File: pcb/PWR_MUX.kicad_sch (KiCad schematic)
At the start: 6 parts, among them IC7 TPS2121RUXT

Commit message: power done
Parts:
- added JP3: SolderJumper_2_Bridged, Jumper:SolderJumper-2_P1.3mm_Bridged_RoundedPad1.0x1.5mm, symbol Jumper:SolderJumper_2_Bridged
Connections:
- net GND: now also JP3.2 (B); no longer IC7.3 (CP2)
- new net: IC7.3 (CP2), JP3.1 (A)
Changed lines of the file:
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@@
 	(wire
 		(pts
-			(xy 111.76 76.2) (xy 114.3 76.2)
+			(xy 111.76 76.2) (xy 115.57 76.2)
 		)
 		(stroke
@@
 		(pts
 			(xy 76.2 60.96) (xy 83.82 60.96)
+		)
+		(stroke
+			(width 0)
+			(type default)
+		)
+	)
+	(wire
+		(pts
+			(xy 123.19 76.2) (xy 127 76.2)
 		)
 		(stroke
@@
 	(symbol
 		(lib_id "power:GND")
-		(at 114.3 76.2 90)
+		(at 127 76.2 90)
 		(unit 1)
 		(exclude_from_sim no)
@@
 		(dnp no)
 		(property "Reference" "#PWR0306"
-			(at 120.65 76.2 0)
+			(at 133.35 76.2 0)
 			(effects
 				(font
@@
 		)
 		(property "Value" "GND"
-			(at 118.11 76.2 0)
+			(at 130.81 76.2 0)
 			(effects
 				(font
@@
 		)
 		(property "Footprint" ""
-			(at 114.3 76.2 0)
+			(at 127 76.2 0)
 			(effects
 				(font
@@
 		)
 		(property "Datasheet" ""
-			(at 114.3 76.2 0)
+			(at 127 76.2 0)
 			(effects
 				(font
@@
 		)
 		(property "Description" "Power symbol creates a global label with name \"GND\" , ground"
-			(at 114.3 76.2 0)
+			(at 127 76.2 0)
 			(effects
 				(font
@@
 					(unit 1)
 				)
+			)
+		)
+	)
+	(symbol
+		(lib_id "Jumper:SolderJumper_2_Bridged")
+		(at 119.38 76.2 0)
+		(unit 1)
+		(exclude_from_sim no)
+		(in_bom no)
+		(on_board yes)
+		(dnp no)
+		(property "Reference" "JP3"
+			(at 119.38 73.66 0)
+			(effects
+				(font
+					(size 1.27 1.27)
+				)
+			)
+		)
+		(property "Value" "SolderJumper_2_Bridged"
+			(at 119.38 72.39 0)
+			(effects
+				(font
+					(size 1.27 1.27)
+				)
+				(hide yes)
+			)
+		)
+		(property "Footprint" "Jumper:SolderJumper-2_P1.3mm_Bridged_RoundedPad1.0x1.5mm"
+			(at 119.38 76.2 0)
+			(effects
+				(font
+					(size 1.27 1.27)
+				)
+				(hide yes)
+			)
+		)
+		(property "Datasheet" "~"
+			(at 119.38 76.2 0)
+			(effects
+				(font
+					(size 1.27 1.27)
+				)
+				(hide yes)
+			)
+		)
+		(property "Description" "Solder Jumper, 2-pole, closed/bridged"
+			(at 119.38 76.2 0)
+			(effects
+				(font
+					(size 1.27 1.27)
+				)
+				(hide yes)
+			)
+		)
+		(pin "1"
+		)
+		(pin "2"
+		)
+		(instances
+			(project ""
+				(path "/3aee14c3-5480-4f7c-989e-3fef81779034/05e3be97-98f6-4518-a1a7-240d4da327e6/d1a8c66e-d7c5-4f43-8cdd-a3ddabbe33e6"
+					(reference "JP3")
+					(unit 1)
+				)

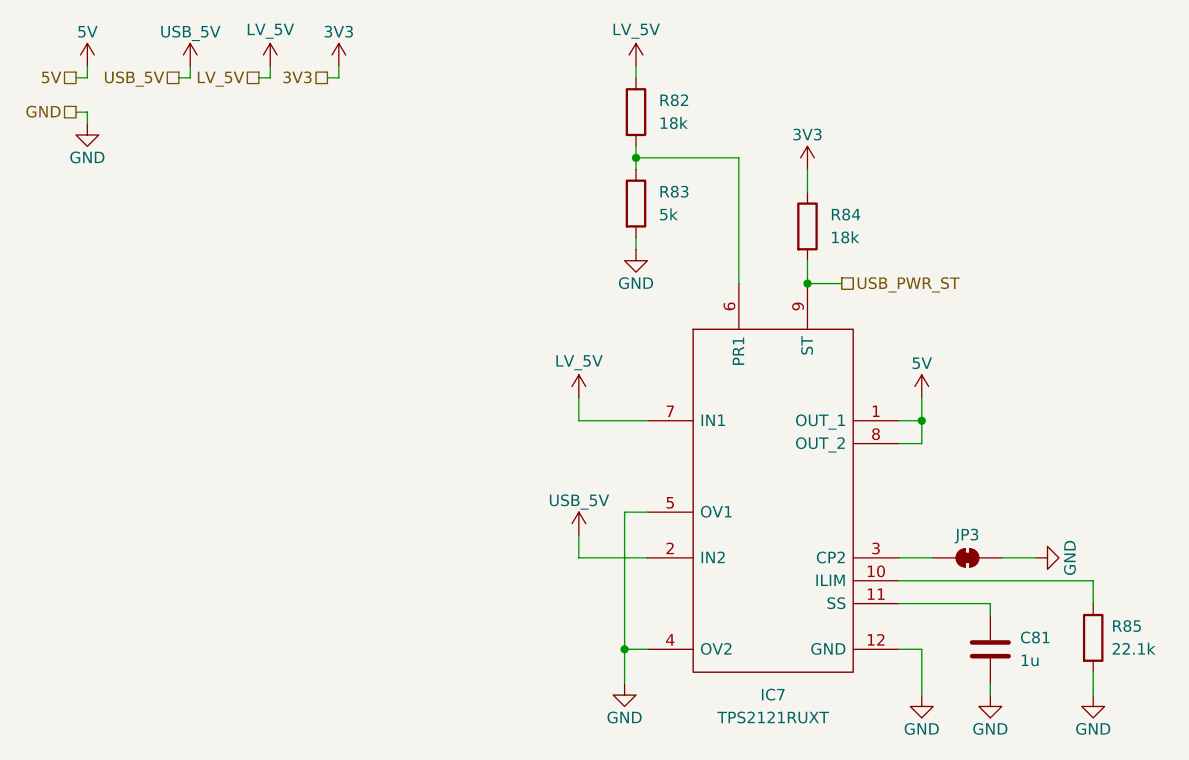
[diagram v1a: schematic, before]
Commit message: reannotated, updated some symbols
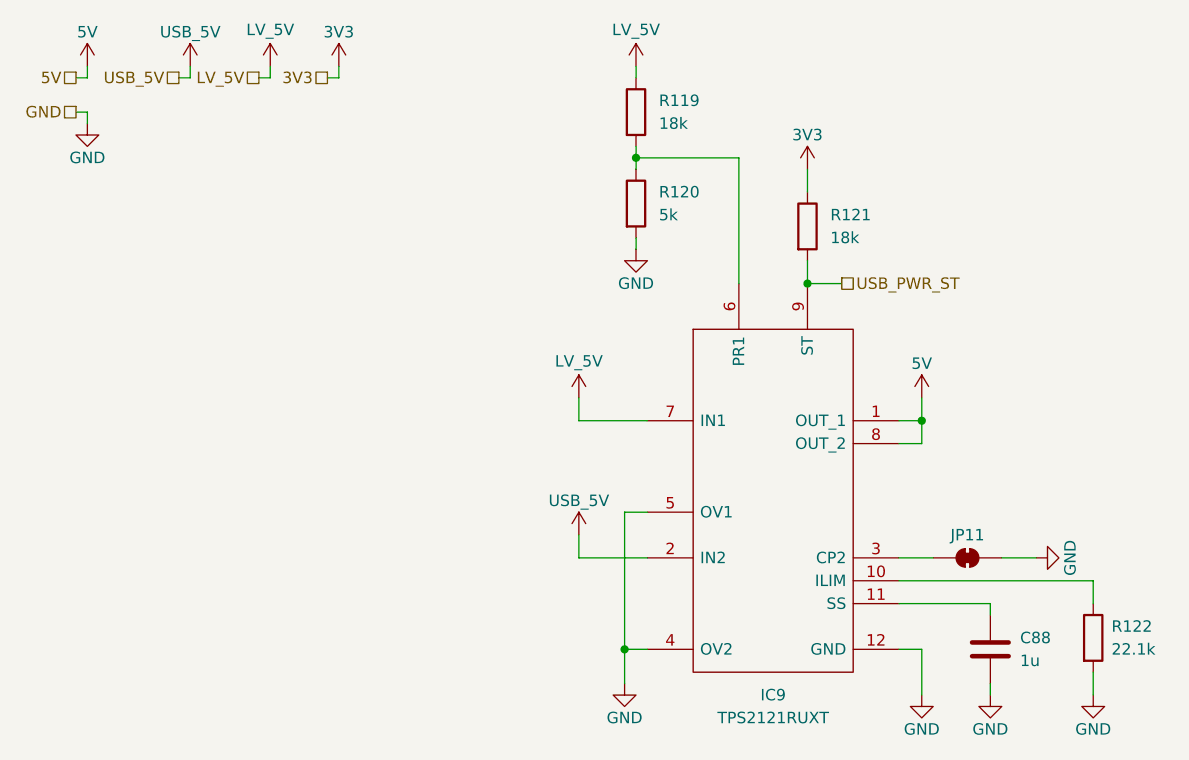
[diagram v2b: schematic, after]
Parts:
- renumbered C81 to C88, IC7 to IC9, JP3 to JP11, R82 to R119, R83 to R120, R84 to R121, R85 to R122
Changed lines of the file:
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@@
 		(on_board yes)
 		(dnp no)
-		(property "Reference" "C81"
+		(property "Reference" "C88"
 			(at 125.222 85.09 0)
 			(effects
@@
 			(project ""
 				(path "/3aee14c3-5480-4f7c-989e-3fef81779034/05e3be97-98f6-4518-a1a7-240d4da327e6/d1a8c66e-d7c5-4f43-8cdd-a3ddabbe33e6"
-					(reference "C81")
+					(reference "C88")
 					(unit 1)
 				)
@@
 		(dnp no)
 		(fields_autoplaced yes)
-		(property "Reference" "R84"
+		(property "Reference" "R121"
 			(at 104.14 38.0999 0)
 			(effects
@@
 			(project "NCU"
 				(path "/3aee14c3-5480-4f7c-989e-3fef81779034/05e3be97-98f6-4518-a1a7-240d4da327e6/d1a8c66e-d7c5-4f43-8cdd-a3ddabbe33e6"
-					(reference "R84")
+					(reference "R121")
 					(unit 1)
 				)
@@
 		(on_board yes)
 		(dnp no)
-		(property "Reference" "#PWR0303"
+		(property "Reference" "#PWR0399"
 			(at 82.55 48.26 0)
 			(effects
@@
 			(project "NCU"
 				(path "/3aee14c3-5480-4f7c-989e-3fef81779034/05e3be97-98f6-4518-a1a7-240d4da327e6/d1a8c66e-d7c5-4f43-8cdd-a3ddabbe33e6"
-					(reference "#PWR0303")
+					(reference "#PWR0399")
 					(unit 1)
 				)
@@
 		(on_board yes)
 		(dnp no)
-		(property "Reference" "#PWR0306"
+		(property "Reference" "#PWR0404"
 			(at 133.35 76.2 0)
 			(effects
@@
 			(project "NCU"
 				(path "/3aee14c3-5480-4f7c-989e-3fef81779034/05e3be97-98f6-4518-a1a7-240d4da327e6/d1a8c66e-d7c5-4f43-8cdd-a3ddabbe33e6"
-					(reference "#PWR0306")
+					(reference "#PWR0404")
 					(unit 1)
 				)
@@
 		(on_board yes)
 		(dnp no)
-		(property "Reference" "#PWR0294"
+		(property "Reference" "#PWR0390"
 			(at 21.59 25.4 0)
 			(effects
@@
 			(project "NCU"
 				(path "/3aee14c3-5480-4f7c-989e-3fef81779034/05e3be97-98f6-4518-a1a7-240d4da327e6/d1a8c66e-d7c5-4f43-8cdd-a3ddabbe33e6"
-					(reference "#PWR0294")
+					(reference "#PWR0390")
 					(unit 1)
 				)
@@
 		(on_board yes)
 		(dnp no)
-		(property "Reference" "#PWR0308"
+		(property "Reference" "#PWR0403"
 			(at 121.92 97.79 0)
 			(effects
@@
 			(project "NCU"
 				(path "/3aee14c3-5480-4f7c-989e-3fef81779034/05e3be97-98f6-4518-a1a7-240d4da327e6/d1a8c66e-d7c5-4f43-8cdd-a3ddabbe33e6"
-					(reference "#PWR0308")
+					(reference "#PWR0403")
 					(unit 1)
 				)
@@
 		(on_board yes)
 		(dnp no)
-		(property "Reference" "#PWR0304"
+		(property "Reference" "#PWR0400"
 			(at 101.6 36.83 0)
 			(effects
@@
 			(project "NCU"
 				(path "/3aee14c3-5480-4f7c-989e-3fef81779034/05e3be97-98f6-4518-a1a7-240d4da327e6/d1a8c66e-d7c5-4f43-8cdd-a3ddabbe33e6"
-					(reference "#PWR0304")
+					(reference "#PWR0400")
 					(unit 1)
 				)
@@
 		(on_board yes)
 		(dnp no)
-		(property "Reference" "#PWR0307"
+		(property "Reference" "#PWR0402"
 			(at 114.3 97.79 0)
 			(effects
@@
 			(project "NCU"
 				(path "/3aee14c3-5480-4f7c-989e-3fef81779034/05e3be97-98f6-4518-a1a7-240d4da327e6/d1a8c66e-d7c5-4f43-8cdd-a3ddabbe33e6"
-					(reference "#PWR0307")
+					(reference "#PWR0402")
 					(unit 1)
 				)
@@
 		(on_board yes)
 		(dnp no)
-		(property "Reference" "R85"
+		(property "Reference" "R122"
 			(at 135.382 83.82 0)
 			(effects
@@
 			(project "NCU"
 				(path "/3aee14c3-5480-4f7c-989e-3fef81779034/05e3be97-98f6-4518-a1a7-240d4da327e6/d1a8c66e-d7c5-4f43-8cdd-a3ddabbe33e6"
-					(reference "R85")
+					(reference "R122")
 					(unit 1)
 				)
@@
 		(on_board yes)
 		(dnp no)
-		(property "Reference" "JP3"
+		(property "Reference" "JP11"
 			(at 119.38 73.66 0)
 			(effects
@@
 			(project ""
 				(path "/3aee14c3-5480-4f7c-989e-3fef81779034/05e3be97-98f6-4518-a1a7-240d4da327e6/d1a8c66e-d7c5-4f43-8cdd-a3ddabbe33e6"
-					(reference "JP3")
+					(reference "JP11")
 					(unit 1)
 				)
@@
 		(on_board yes)
 		(dnp no)
-		(property "Reference" "#PWR0302"
+		(property "Reference" "#PWR0398"
 			(at 82.55 25.4 0)
 			(effects
@@
 			(project "NCU"
 				(path "/3aee14c3-5480-4f7c-989e-3fef81779034/05e3be97-98f6-4518-a1a7-240d4da327e6/d1a8c66e-d7c5-4f43-8cdd-a3ddabbe33e6"
-					(reference "#PWR0302")
+					(reference "#PWR0398")
 					(unit 1)
 				)
@@
 		(on_board yes)
 		(dnp no)
-		(property "Reference" "#PWR0309"
+		(property "Reference" "#PWR0405"
 			(at 133.35 97.79 0)
 			(effects
@@
 			(project "NCU"
 				(path "/3aee14c3-5480-4f7c-989e-3fef81779034/05e3be97-98f6-4518-a1a7-240d4da327e6/d1a8c66e-d7c5-4f43-8cdd-a3ddabbe33e6"
-					(reference "#PWR0309")
+					(reference "#PWR0405")
 					(unit 1)
 				)
@@
 		(dnp no)
 		(fields_autoplaced yes)
-		(property "Reference" "R83"
+		(property "Reference" "R120"
 			(at 85.09 35.5599 0)
 			(effects
@@
 			(project "NCU"
 				(path "/3aee14c3-5480-4f7c-989e-3fef81779034/05e3be97-98f6-4518-a1a7-240d4da327e6/d1a8c66e-d7c5-4f43-8cdd-a3ddabbe33e6"
-					(reference "R83")
+					(reference "R120")
 					(unit 1)
 				)
@@
 		(on_board yes)
 		(dnp no)
-		(property "Reference" "#PWR0298"
+		(property "Reference" "#PWR0394"
 			(at 49.53 25.4 0)
 			(effects
@@
 			(project "NCU"
 				(path "/3aee14c3-5480-4f7c-989e-3fef81779034/05e3be97-98f6-4518-a1a7-240d4da327e6/d1a8c66e-d7c5-4f43-8cdd-a3ddabbe33e6"
-					(reference "#PWR0298")
+					(reference "#PWR0394")
 					(unit 1)
 				)
@@
 		(on_board yes)
 		(dnp no)
-		(property "Reference" "#PWR0297"
+		(property "Reference" "#PWR0393"
 			(at 41.91 25.4 0)
 			(effects
@@
 			(project "NCU"
 				(path "/3aee14c3-5480-4f7c-989e-3fef81779034/05e3be97-98f6-4518-a1a7-240d4da327e6/d1a8c66e-d7c5-4f43-8cdd-a3ddabbe33e6"
-					(reference "#PWR0297")
+					(reference "#PWR0393")
 					(unit 1)
 				)
@@
 		(dnp no)
 		(fields_autoplaced yes)
-		(property "Reference" "R82"
+		(property "Reference" "R119"
 			(at 85.09 25.3999 0)
 			(effects
@@
 			(project ""
 				(path "/3aee14c3-5480-4f7c-989e-3fef81779034/05e3be97-98f6-4518-a1a7-240d4da327e6/d1a8c66e-d7c5-4f43-8cdd-a3ddabbe33e6"
-					(reference "R82")
+					(reference "R119")
 					(unit 1)
 				)
@@
 		(dnp no)
 		(fields_autoplaced yes)
-		(property "Reference" "IC7"
+		(property "Reference" "IC9"
 			(at 97.79 91.44 0)
 			(effects
@@
 			(project ""
 				(path "/3aee14c3-5480-4f7c-989e-3fef81779034/05e3be97-98f6-4518-a1a7-240d4da327e6/d1a8c66e-d7c5-4f43-8cdd-a3ddabbe33e6"
-					(reference "IC7")
+					(reference "IC9")
 					(unit 1)
 				)
@@
 		(on_board yes)
 		(dnp no)
-		(property "Reference" "#PWR0299"
+		(property "Reference" "#PWR0395"
 			(at 76.2 62.23 0)
 			(effects
@@
 			(project "NCU"
 				(path "/3aee14c3-5480-4f7c-989e-3fef81779034/05e3be97-98f6-4518-a1a7-240d4da327e6/d1a8c66e-d7c5-4f43-8cdd-a3ddabbe33e6"
-					(reference "#PWR0299")
+					(reference "#PWR0395")
 					(unit 1)
 				)
@@
 		(on_board yes)
 		(dnp no)
-		(property "Reference" "#PWR0296"
+		(property "Reference" "#PWR0392"
 			(at 33.02 25.4 0)
 			(effects
@@
 			(project "NCU"
 				(path "/3aee14c3-5480-4f7c-989e-3fef81779034/05e3be97-98f6-4518-a1a7-240d4da327e6/d1a8c66e-d7c5-4f43-8cdd-a3ddabbe33e6"
-					(reference "#PWR0296")
+					(reference "#PWR0392")
 					(unit 1)
 				)
@@
 		(on_board yes)
 		(dnp no)
-		(property "Reference" "#PWR0301"
+		(property "Reference" "#PWR0397"
 			(at 81.28 96.52 0)
 			(effects
@@
 			(project "NCU"
 				(path "/3aee14c3-5480-4f7c-989e-3fef81779034/05e3be97-98f6-4518-a1a7-240d4da327e6/d1a8c66e-d7c5-4f43-8cdd-a3ddabbe33e6"
-					(reference "#PWR0301")
+					(reference "#PWR0397")
 					(unit 1)
 				)
@@
 		(on_board yes)
 		(dnp no)
-		(property "Reference" "#PWR0295"
+		(property "Reference" "#PWR0391"
 			(at 21.59 34.29 0)
 			(effects
@@
 			(project "NCU"
 				(path "/3aee14c3-5480-4f7c-989e-3fef81779034/05e3be97-98f6-4518-a1a7-240d4da327e6/d1a8c66e-d7c5-4f43-8cdd-a3ddabbe33e6"
-					(reference "#PWR0295")
+					(reference "#PWR0391")
 					(unit 1)
 				)
@@
 		(on_board yes)
 		(dnp no)
-		(property "Reference" "#PWR0305"
+		(property "Reference" "#PWR0401"
 			(at 114.3 62.23 0)
 			(effects
@@
 			(project "NCU"
 				(path "/3aee14c3-5480-4f7c-989e-3fef81779034/05e3be97-98f6-4518-a1a7-240d4da327e6/d1a8c66e-d7c5-4f43-8cdd-a3ddabbe33e6"
-					(reference "#PWR0305")
+					(reference "#PWR0401")
 					(unit 1)
 				)
@@
 		(on_board yes)
 		(dnp no)
-		(property "Reference" "#PWR0300"
+		(property "Reference" "#PWR0396"
 			(at 76.2 77.47 0)
 			(effects
@@
 			(project "NCU"
 				(path "/3aee14c3-5480-4f7c-989e-3fef81779034/05e3be97-98f6-4518-a1a7-240d4da327e6/d1a8c66e-d7c5-4f43-8cdd-a3ddabbe33e6"
-					(reference "#PWR0300")
-					(unit 1)
-				)
+					(reference "#PWR0396")
+					(unit 1)
+				)

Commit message: minor changes before layout
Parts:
- added C96: 1u, Capacitor_SMD:C_0603_1608Metric, symbol Device:C
- added C97: 100n, Capacitor_SMD:C_0603_1608Metric, symbol Device:C
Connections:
- net GND: now also C96.2, C97.2
- net USB_5V: now also C96.1, C97.1
